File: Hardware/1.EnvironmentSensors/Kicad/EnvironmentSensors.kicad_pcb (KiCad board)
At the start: 2 copper layers, 70 x 70 mm, 16 parts, among them J1 Conn_01x10_Pin, J3 Conn_01x10_Pin, U1 SHT4x, U2 BME680, U3 LPS22HB

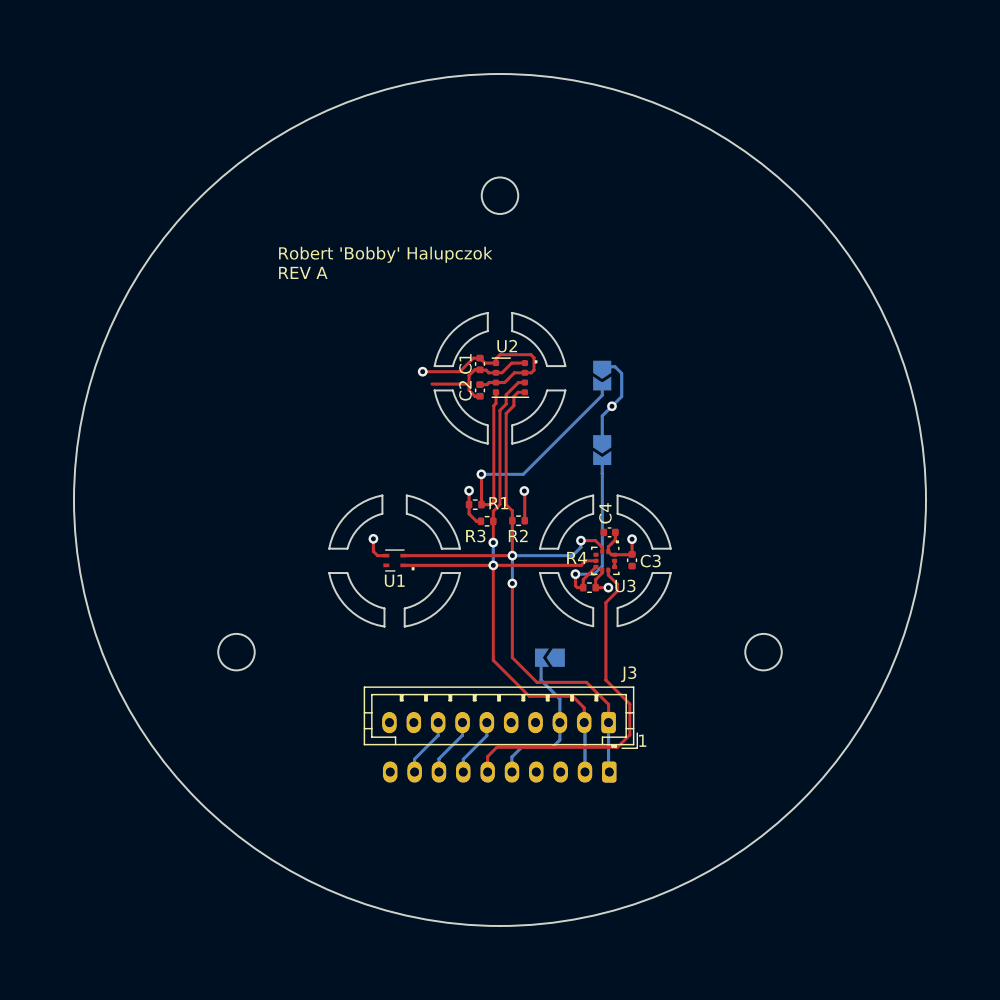
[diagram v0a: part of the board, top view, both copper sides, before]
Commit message: Modify PCB layout
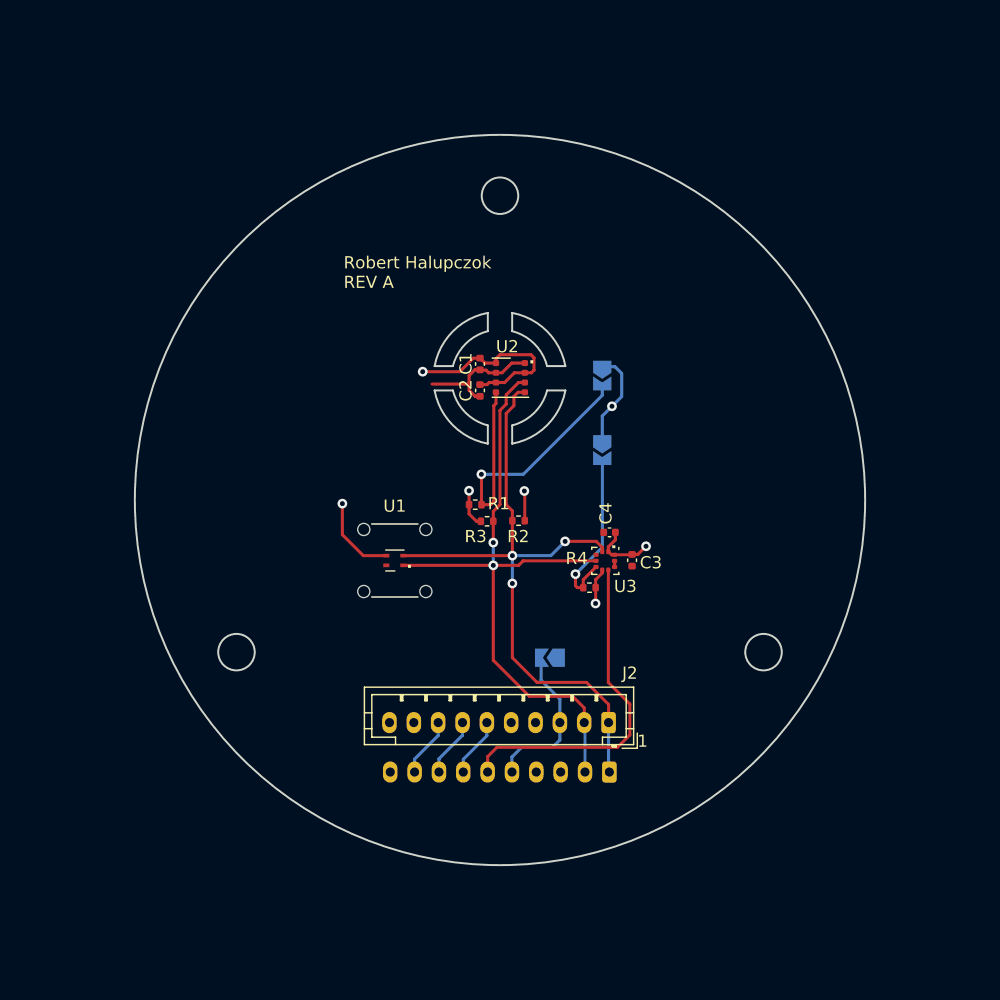
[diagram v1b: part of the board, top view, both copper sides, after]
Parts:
- added FL1: SF2_FILTER_CAP, FIL_SF2_FILTER_CAP:FIL_SF2_FILTER_CAP, F.Cu at (126.7, 90.5)
- J1: footprint Connector_JST:JST_PH_S10B-PH-K_1x10_P2.00mm_Horizontal -> Connector_JST:JST_PH_B10B-PH-K_1x10_P2.00mm_Vertical
- renumbered J3 to J2
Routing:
- net +3.3V: track 31.9 -> 37.0 mm
- net Net-(JP2-B): track 15.1 -> 14.2 mm
- net LPS22HB_INT: track 28.7 -> 28.0 mm
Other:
- board size 70 x 70 mm -> 60 x 60 mm
- board text added: "BME680 Address 0x76 - Closed 0x77 - Open"
- board text added: "LPS22HB Address 0x5C - Closed 0x5D - Open"
- board text added: "Robert Halupczok REV A"
- board text removed: "BME680 Address: 0x76 - Closed 0x77 - Open"
- board text removed: "LPS22HB Address: 0x5C - Closed 0x5D - Open"
- board text removed: "Robert 'Bobby' Halupczok REV A"

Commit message: Update pcb due to conector change
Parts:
- FL1: value SF2_FILTER_CAP -> Sht45 Filter
- J1, J2: footprint Connector_JST:JST_PH_B10B-PH-K_1x10_P2.00mm_Vertical -> Connector_JST:JST_PH_B10B-PH-SM4-TB_1x10-1MP_P2.00mm_Vertical
- moved J1 9.38 mm to (135.3, 105.2), turned to 0 degrees
- moved J2 9.02 mm to (135.3, 105.2), turned to 0 degrees
- moved JP3 4.48 mm to (138.9, 94.0)
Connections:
- J2 pad 6: EXT_OPT3004_INT -> unconnected-(J2-Pin_6-Pad6)
- J2 pad 7: EXT_AS7331_SYN -> EXT_OPT3004_INT
- J2 pad 8: EXT_AS7331_READY -> EXT_AS7331_SYN
- J2 pad 9: unconnected-(J2-Pin_9-Pad9) -> EXT_AS7331_READY
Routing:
- net EXT_3V3: track 13.2 -> 30.1 mm, vias 0 -> 1
- net LPS22HB_INT: track 28.0 -> 20.1 mm, vias 0 -> 1
- net I2C_SDA: track 54.5 -> 47.9 mm, vias 2 -> 3
- net EXT_AS7331_READY: track 4.87 -> 0.00 mm, vias 0 -> 1
- net EXT_OPT3004_INT: track 4.87 -> 0.00 mm, vias 0 -> 1
- net EXT_AS7331_SYN: track 4.87 -> 0.00 mm, vias 0 -> 1
- net I2C_SCL: track 55.3 -> 51.9 mm
- net GND: vias 1 -> 2
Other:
- board text added: "3V3"
- board text added: "AS7331_READY"
- board text added: "AS7331_SYN"
- board text added: "EXT_3V3"
- board text added: "GND"
- board text added: "LPS22HB_INT"
- board text added: "OPT3004_INT"
- board text added: "SCL"
- board text added: "SDA"

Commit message: Add project logo and update silkscreen
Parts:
- added REF**: MORS_logo, MORS_logo:MORS_logo, F.Cu at (124.2, 82.2)
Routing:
- net +3.3V: track 37.1 -> 37.8 mm
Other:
- board text added: "M.O.R.S"
- board text added: "Project: M.O.R.S PCB: Environment Sensors Revision: A Author: Robert Halupczok GitHub: L0R3nz"
- board text removed: "Robert Halupczok REV A"
